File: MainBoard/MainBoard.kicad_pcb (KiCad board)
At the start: 6 copper layers, 45 x 45.6 mm, 56 parts, among them IC1 BQ25171QWDRCRQ1, J1 KH-TYPE-C-16P, U1 STM32L496VGY6PTR, U2 MX25R1635FZUIL0, U3 SI3477DV-T1-GE3, U4 SI3477DV-T1-GE3, U5 TPS63802DLAR, U6 FUSB302BMPX, U7 BNO086, Y1 9HT11-32.768KBZF-T

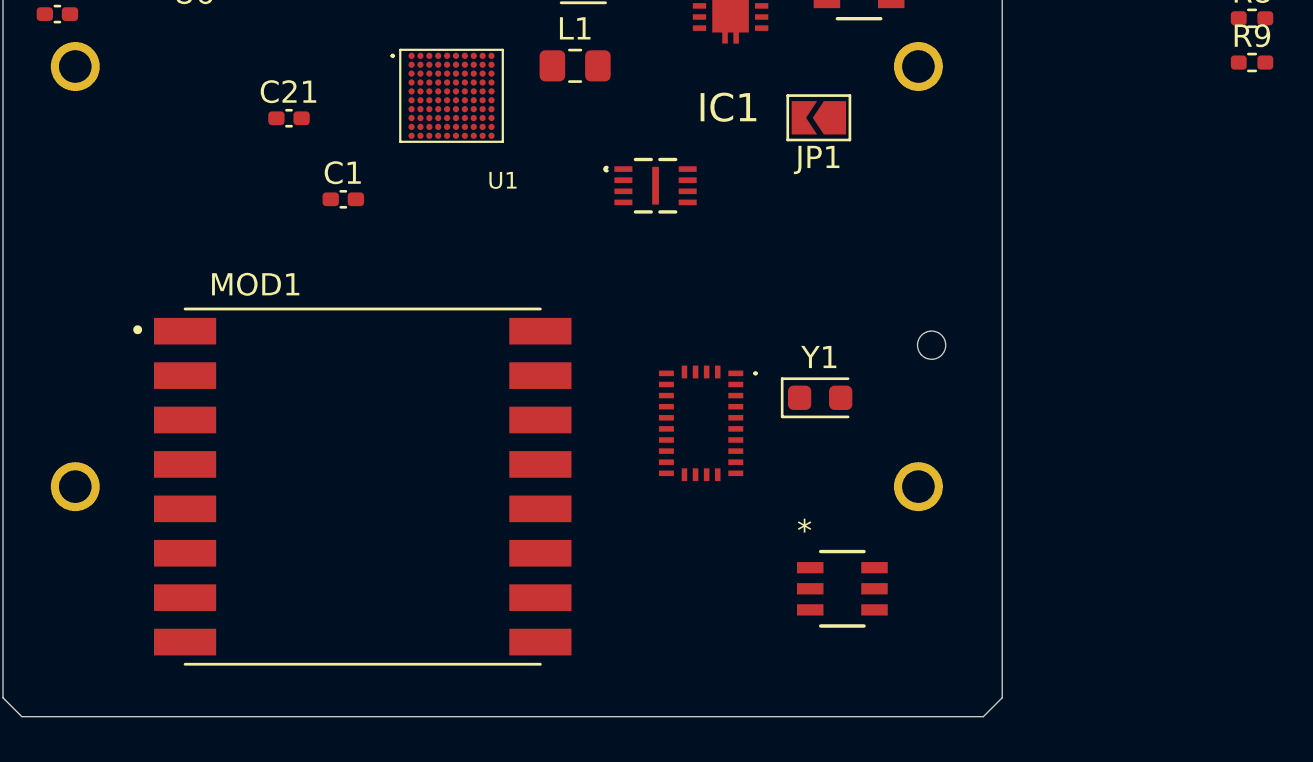
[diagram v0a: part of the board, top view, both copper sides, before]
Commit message: Add CAN transceiver - removed radio module
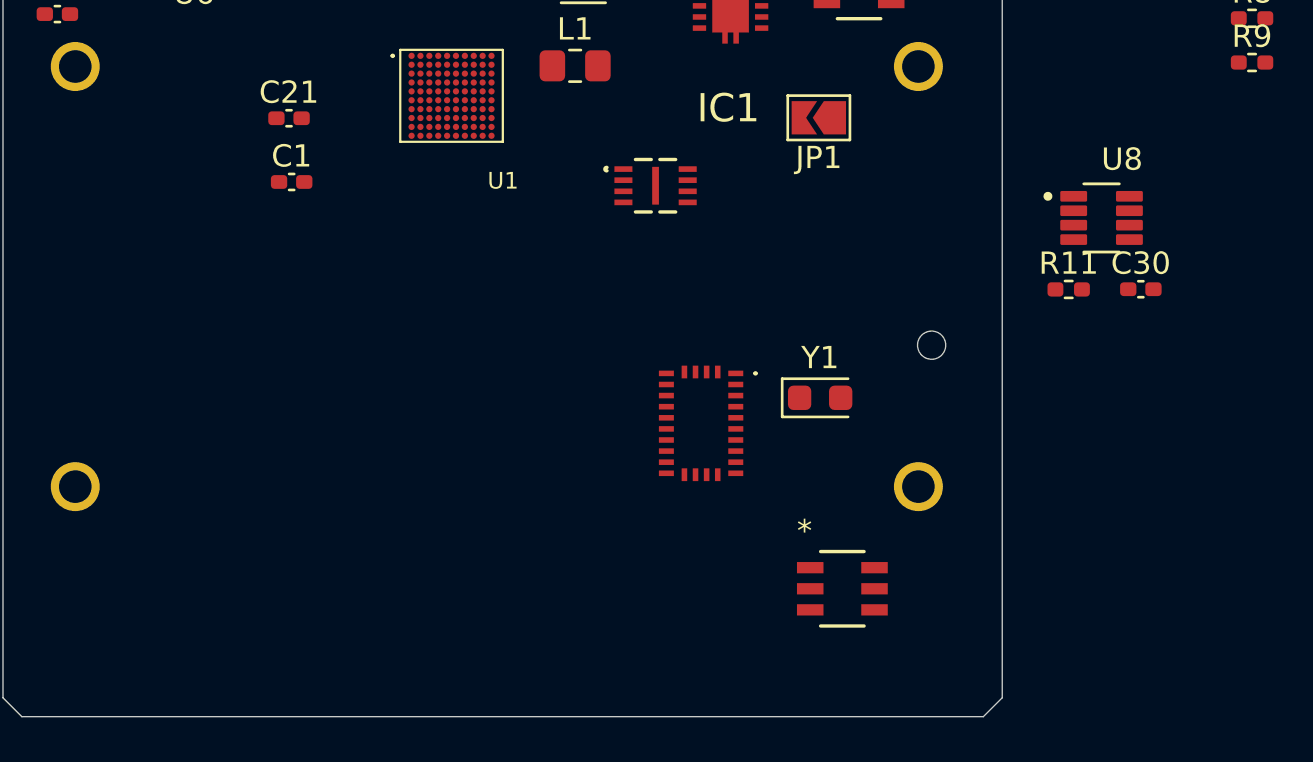
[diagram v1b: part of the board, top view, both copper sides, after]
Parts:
- removed MOD1: RFM98W-433S2, inspirefly:XCVR_RFM98W-433S2
- added C30: 100nF, Capacitor_SMD:C_0402_1005Metric_Pad0.74x0.62mm_HandSolder, F.Cu at (120.6, 67.5)
- added R11: 120, Resistor_SMD:R_0402_1005Metric_Pad0.72x0.64mm_HandSolder, F.Cu at (117.4, 67.5)
- added U8: TCAN332DCNR, inspirefly:SOT65P280X145-8N, F.Cu at (118.9, 64.3)
- moved C1 2.45 mm to (82.4, 62.7)
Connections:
- U1 pad C9: unconnected-(U1A-PC13-PadC9) -> IMU_H_INTN_GPIO
- U1 pad G8: unconnected-(U1A-PA0-PadG8) -> IMU_PS0/WAKE_GPIO
- U7 pad 14: unconnected-(U7-H_INTN-Pad14) -> IMU_H_INTN_GPIO
- U7 pad 6: unconnected-(U7-PS0/WAKE-Pad6) -> IMU_PSO/WAKE_GPIO

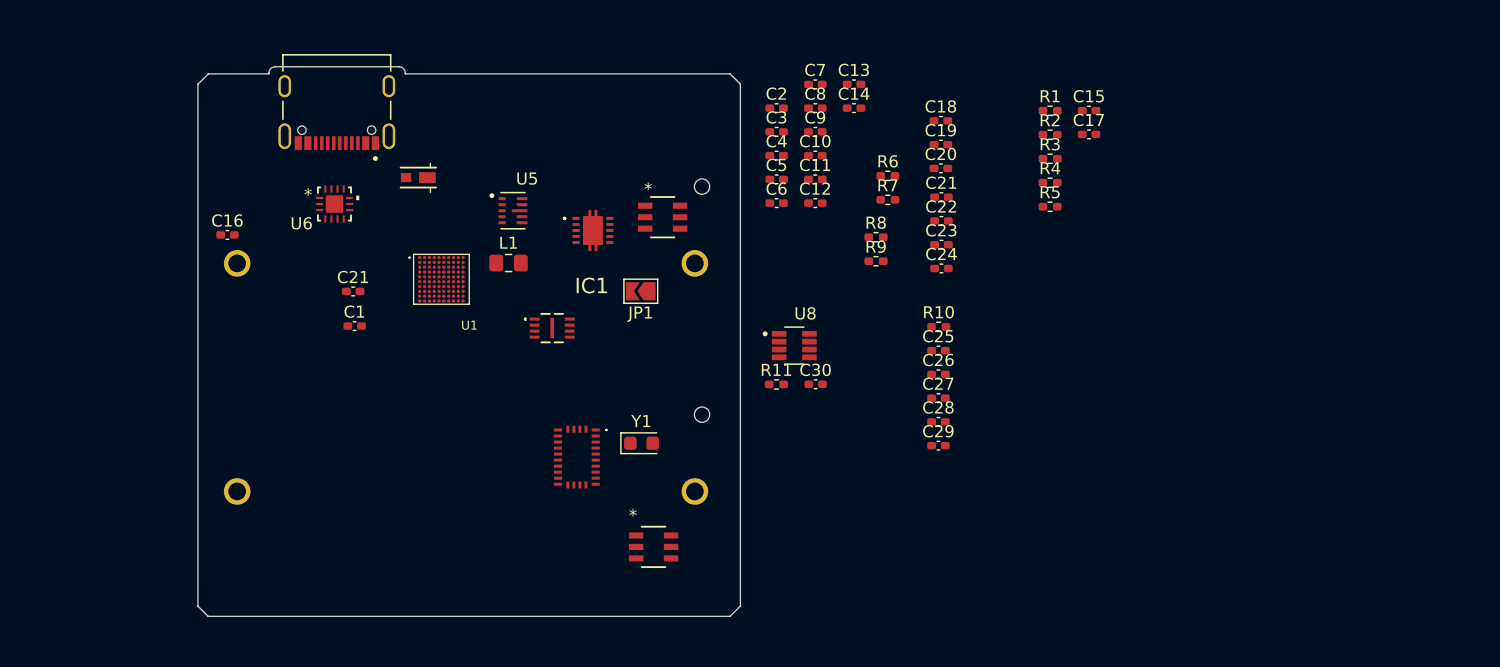
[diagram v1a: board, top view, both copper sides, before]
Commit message: Integrated BQ25756E along with schematic changes
Removed old Battery management, replaced with BQ25756E. Schematic work complete along with external part finding.
Dedicated section to I2C pull ups.
Moved around items in schematics for better look.
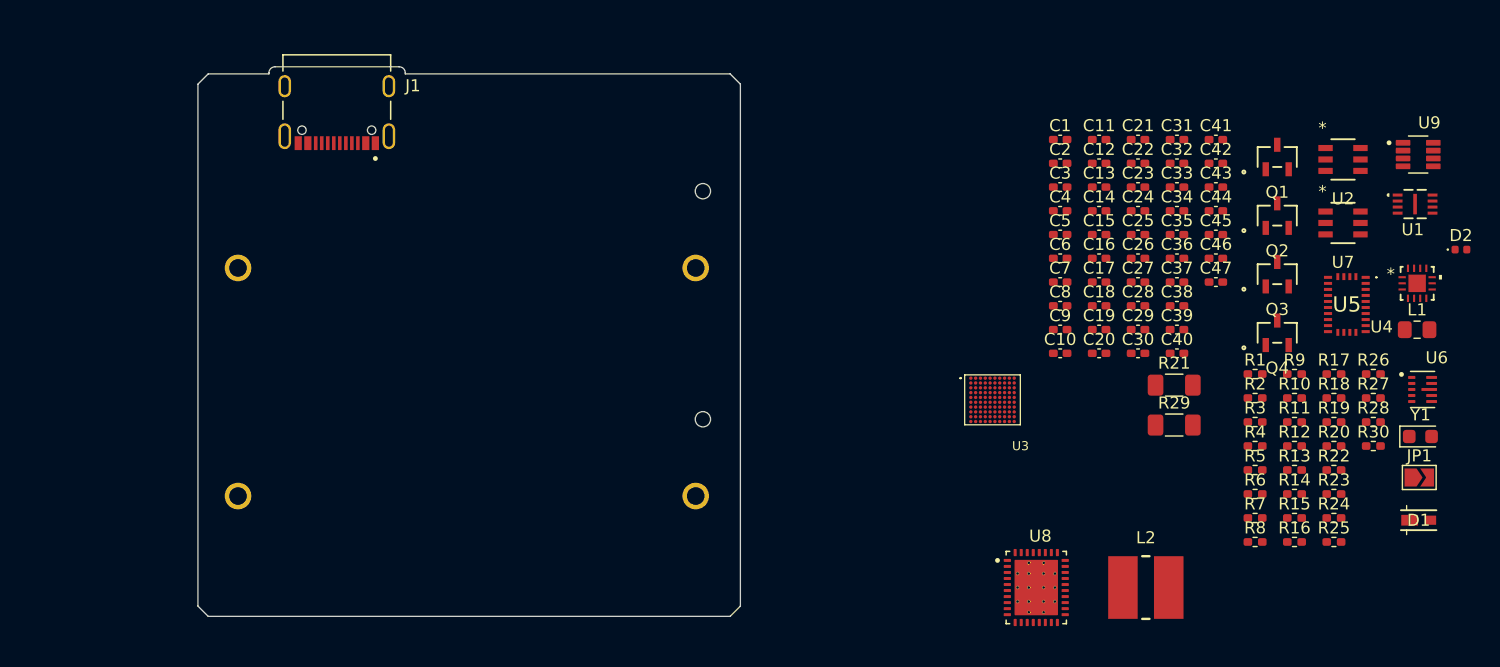
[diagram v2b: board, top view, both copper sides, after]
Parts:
- removed the C21 at (82.3, 59.8)
- removed the C21 at (131.1, 52.0)
- removed IC1: BQ25171QWDRCRQ1, inspirefly:BQ25171QWDRCRQ1
- added C21: 100nF, Capacitor_SMD:C_0402_1005Metric_Pad0.74x0.62mm_HandSolder, F.Cu at (147.4, 47.2)
- added C31: 470nF, Capacitor_SMD:C_0402_1005Metric_Pad0.74x0.62mm_HandSolder, F.Cu at (150.6, 47.2)
- added C32: 100nF, Capacitor_SMD:C_0402_1005Metric_Pad0.74x0.62mm_HandSolder, F.Cu at (150.6, 49.2)
- added C33: 100nF, Capacitor_SMD:C_0402_1005Metric_Pad0.74x0.62mm_HandSolder, F.Cu at (150.6, 51.1)
- added C34: 22uF, Capacitor_SMD:C_0402_1005Metric_Pad0.74x0.62mm_HandSolder, F.Cu at (150.6, 53.1)
- added C35: 22uF, Capacitor_SMD:C_0402_1005Metric_Pad0.74x0.62mm_HandSolder, F.Cu at (150.6, 55.1)
- added C36: 4.7uF, Capacitor_SMD:C_0402_1005Metric_Pad0.74x0.62mm_HandSolder, F.Cu at (150.6, 57.1)
- added C37: 4.7uF, Capacitor_SMD:C_0402_1005Metric_Pad0.74x0.62mm_HandSolder, F.Cu at (150.6, 59.0)
- added C38: 1uF, Capacitor_SMD:C_0402_1005Metric_Pad0.74x0.62mm_HandSolder, F.Cu at (150.6, 61.0)
- added C39: 22uF, Capacitor_SMD:C_0402_1005Metric_Pad0.74x0.62mm_HandSolder, F.Cu at (150.6, 63.0)
- added C40: 22uF, Capacitor_SMD:C_0402_1005Metric_Pad0.74x0.62mm_HandSolder, F.Cu at (150.6, 64.9)
- added C41: 100nF, Capacitor_SMD:C_0402_1005Metric_Pad0.74x0.62mm_HandSolder, F.Cu at (153.8, 47.2)
- added C42: 100nF, Capacitor_SMD:C_0402_1005Metric_Pad0.74x0.62mm_HandSolder, F.Cu at (153.8, 49.2)
- added C43: 100nF, Capacitor_SMD:C_0402_1005Metric_Pad0.74x0.62mm_HandSolder, F.Cu at (153.8, 51.1)
- added C44: 470nF, Capacitor_SMD:C_0402_1005Metric_Pad0.74x0.62mm_HandSolder, F.Cu at (153.8, 53.1)
- added C45: 100nF, Capacitor_SMD:C_0402_1005Metric_Pad0.74x0.62mm_HandSolder, F.Cu at (153.8, 55.1)
- added C46: 22uF, Capacitor_SMD:C_0402_1005Metric_Pad0.74x0.62mm_HandSolder, F.Cu at (153.8, 57.1)
- added C47: 22uF, Capacitor_SMD:C_0402_1005Metric_Pad0.74x0.62mm_HandSolder, F.Cu at (153.8, 59.0)
- added D2: LED, LED_SMD:LED_0402_1005Metric, F.Cu at (174.2, 56.3)
- added L2: 4.7uH, inspirefly:WE-LQSA_5040, F.Cu at (148.0, 84.4)
- added Q1: PMV19XNEAR, inspirefly:TO-236AB_SOT23_NEX, F.Cu at (158.9, 48.7)
- added Q2: PMV19XNEAR, inspirefly:TO-236AB_SOT23_NEX, F.Cu at (158.9, 53.5)
- added Q3: PMV19XNEAR, inspirefly:TO-236AB_SOT23_NEX, F.Cu at (158.9, 58.4)
- added Q4: PMV19XNEAR, inspirefly:TO-236AB_SOT23_NEX, F.Cu at (158.9, 63.2)
- added R12: 50k, Resistor_SMD:R_0402_1005Metric_Pad0.72x0.64mm_HandSolder, F.Cu at (160.4, 72.6)
- added R13: 100K, Resistor_SMD:R_0402_1005Metric_Pad0.72x0.64mm_HandSolder, F.Cu at (160.4, 74.6)
- added R14: 143k, Resistor_SMD:R_0402_1005Metric_Pad0.72x0.64mm_HandSolder, F.Cu at (160.4, 76.6)
- added R15: 250k, Resistor_SMD:R_0402_1005Metric_Pad0.72x0.64mm_HandSolder, F.Cu at (160.4, 78.6)
- added R16: 6.2k, Resistor_SMD:R_0402_1005Metric_Pad0.72x0.64mm_HandSolder, F.Cu at (160.4, 80.6)
- added R17: 36k, Resistor_SMD:R_0402_1005Metric_Pad0.72x0.64mm_HandSolder, F.Cu at (163.6, 66.7)
- added R18: 10, Resistor_SMD:R_0402_1005Metric_Pad0.72x0.64mm_HandSolder, F.Cu at (163.6, 68.7)
- added R19: 25k, Resistor_SMD:R_0402_1005Metric_Pad0.72x0.64mm_HandSolder, F.Cu at (163.6, 70.6)
- added R20: 40k, Resistor_SMD:R_0402_1005Metric_Pad0.72x0.64mm_HandSolder, F.Cu at (163.6, 72.6)
- added R21: 5m, Resistor_SMD:R_1206_3216Metric_Pad1.30x1.75mm_HandSolder, F.Cu at (150.4, 67.6)
- added R22: 250k, Resistor_SMD:R_0402_1005Metric_Pad0.72x0.64mm_HandSolder, F.Cu at (163.6, 74.6)
- added R23: 10, Resistor_SMD:R_0402_1005Metric_Pad0.72x0.64mm_HandSolder, F.Cu at (163.6, 76.6)
- added R24: 10k, Resistor_SMD:R_0402_1005Metric_Pad0.72x0.64mm_HandSolder, F.Cu at (163.6, 78.6)
- added R25: 120, Resistor_SMD:R_0402_1005Metric_Pad0.72x0.64mm_HandSolder, F.Cu at (163.6, 80.6)
- added R26: 10k, Resistor_SMD:R_0402_1005Metric_Pad0.72x0.64mm_HandSolder, F.Cu at (166.9, 66.7)
- added R27: 10, Resistor_SMD:R_0402_1005Metric_Pad0.72x0.64mm_HandSolder, F.Cu at (166.9, 68.7)
- added R28: 10, Resistor_SMD:R_0402_1005Metric_Pad0.72x0.64mm_HandSolder, F.Cu at (166.9, 70.6)
- added R29: 5m, Resistor_SMD:R_1206_3216Metric_Pad1.30x1.75mm_HandSolder, F.Cu at (150.4, 70.9)
- added R30: 10, Resistor_SMD:R_0402_1005Metric_Pad0.72x0.64mm_HandSolder, F.Cu at (166.9, 72.6)
- added U9: TCAN332DCNR, inspirefly:SOT65P280X145-8N, F.Cu at (170.6, 48.5)
- C1, C16: value 100nF -> 1uF
- C11: value 100nF -> 4.7uF
- C12, C13, C15, C17: value 1uF -> 100nF
- C19: value 10uF -> 1uF
- C20: value 10uF -> 100nF
- C23: value 470pF -> 100nF
- C24: value 470pF -> 22pF
- C25: value 100nF -> 22pF
- C26, C27: value 100nF -> 10uF
- C28, C29: value 22pF -> 22uF
- C6: value 100nF -> 470pF
- C7: value 4.7uF -> 470pF
- R1: value 10k -> 2.2k
- R11: value 120 -> 280k
- R2: value 375 -> 2.2k
- R3: value 18k -> 2.2k
- R4: value 62k -> 2.2k
- R5: value 100K -> 2.2k
- R6: value 280k -> 2.2k
- R7: value 50k -> 2.2k
- R8, R9: value 4.7k -> 2.2k
- U1: value STM32L496VGY6PTR -> MX25R1635FZUIL0; footprint inspirefly:STM32L496VGY6TR -> inspirefly:USON-8L-2X3X0P6_MAC
- U2: value MX25R1635FZUIL0 -> SI3477DV-T1-GE3; footprint inspirefly:USON-8L-2X3X0P6_MAC -> inspirefly:SOT_V-T1-GE3_VIS-M
- U3: value SI3477DV-T1-GE3 -> STM32L496VGY6PTR; footprint inspirefly:SOT_V-T1-GE3_VIS-M -> inspirefly:STM32L496VGY6TR
- U4: value SI3477DV-T1-GE3 -> FUSB302BMPX; footprint inspirefly:SOT_V-T1-GE3_VIS-M -> inspirefly:MLP14_2P5X2P5_ONS
- U5: value TPS63802DLAR -> BNO086; footprint inspirefly:VREG_TPS63802DLAR -> inspirefly:BNO086
- U6: value FUSB302BMPX -> TPS63802DLAR; footprint inspirefly:MLP14_2P5X2P5_ONS -> inspirefly:VREG_TPS63802DLAR
- U7: value BNO086 -> SI3477DV-T1-GE3; footprint inspirefly:BNO086 -> inspirefly:SOT_V-T1-GE3_VIS-M
- U8: value TCAN332DCNR -> BQ25756ERRVR; footprint inspirefly:SOT65P280X145-8N -> inspirefly:IC_BQ25756ERRVR
- moved U6 91.6 mm to (171.0, 67.9)
- moved D1 87.7 mm to (170.7, 78.8), turned to 0 degrees
- moved U1 81.0 mm to (170.4, 52.6)
- moved L1 75.6 mm to (170.5, 63.0)
- moved C16 72.3 mm to (144.2, 57.1)
- moved U5 69.6 mm to (164.7, 60.9)
- moved U2 67.1 mm to (164.4, 48.9)
- moved U4 67.0 mm to (170.5, 59.1)
- moved U7 66.5 mm to (164.4, 54.1)
- moved JP1 66.4 mm to (170.7, 75.2), turned to 0 degrees
- moved Y1 64.6 mm to (170.8, 71.8)
- moved C1 60.5 mm to (140.9, 47.2)
- moved R11 43.1 mm to (160.4, 70.6)
- moved R8 40.3 mm to (157.1, 80.6)
- moved R6 40.3 mm to (157.1, 76.6)
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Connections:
- BT1 pad P: Net-(U3-S) -> Net-(U7-S)
- BT2 pad P: Net-(U3-S) -> Net-(U7-S)
- C15 pad 1: EXTERNAL_VOLTAGE -> +3.3V
- C16 pad 1: GND -> +3.3V
- C16 pad 2: +3.3V -> GND
- C17 pad 1: BAT+ -> +3.3V
- C23 pad 1: Net-(J1-CC2) -> +3.3V
- C24 pad 1: Net-(J1-CC1) -> Net-(U5-XOUT32/CLKSEL1)
- C25 pad 2: +3.3V -> Net-(U5-XIN32)
- C27 pad 1: Net-(U7-CAP) -> +3.3V
- C28 pad 1: Net-(U7-XOUT32/CLKSEL1) -> EXTERNAL_VOLTAGE
- C29 pad 1: GND -> EXTERNAL_VOLTAGE
- C29 pad 2: Net-(U7-XIN32) -> GND
- C3 pad 1: +3.3V -> GND
- C3 pad 2: GND -> +3.3V
- C30 pad 1: +3.3V -> ACP
- C4 pad 1: +3.3V -> Net-(U5-CAP)
- C5 pad 1: +3.3V -> GND
- C5 pad 2: GND -> +3.3V
- C6 pad 1: +3.3V -> Net-(J1-CC2)
- C7 pad 1: +3.3V -> Net-(J1-CC1)
- L1 pad 1: Net-(U5-L1) -> Net-(U6-L1)
- L1 pad 2: Net-(U5-L2) -> Net-(U6-L2)
- R1 pad 1: GND -> +3.3V
- R1 pad 2: Net-(IC1-TS) -> I2C1_SDA
- R11 pad 1: CAN_L -> +3.3V
- R11 pad 2: CAN_H -> Net-(U6-FB)
- R2 pad 1: GND -> I2C1_SCL
- R2 pad 2: Net-(IC1-ISET) -> +3.3V
- R3 pad 1: Net-(IC1-VSET) -> +3.3V
- R3 pad 2: GND -> I2C2_SDA
- R4 pad 1: Net-(IC1-CHM_TMR) -> I2C2_SCL
- R4 pad 2: GND -> +3.3V
- R5 pad 1: BAT_PULLDOWN -> +3.3V
- R5 pad 2: Net-(U3-S) -> I2C3_SDA
- R6 pad 1: +3.3V -> I2C3_SCL
- R6 pad 2: Net-(U5-FB) -> +3.3V
- R7 pad 1: Net-(U5-FB) -> +3.3V
- R7 pad 2: GND -> I2C3_SDA
- R8 pad 1: I2C1_SCL -> INT_N
- R8 pad 2: GND -> +3.3V
- R9 pad 1: GND -> I2C3_SCL
- R9 pad 2: I2C1_SDA -> +3.3V
- U2 pad 1: QUADSPI_BK2_NCS -> unconnected-(U2-D-Pad1)
- U2 pad 2: QUADSPI_BK2_IO1 -> unconnected-(U2-D-Pad2)
- U2 pad 3: QUADSPI_BK2_IO2 -> unconnected-(U2-G-Pad3)
- U2 pad 4: GND -> unconnected-(U2-S-Pad4)
- U2 pad 5: QUADSPI_BK2_IO0 -> unconnected-(U2-D-Pad5)
- U2 pad 6: QUADSPI_CLK -> unconnected-(U2-D-Pad6)
- U4 pad 2: unconnected-(U4-D-Pad2) -> Net-(D1-A)
- U4 pad 3: unconnected-(U4-G-Pad3) -> +3.3V
- U4 pad 4: unconnected-(U4-S-Pad4) -> +3.3V
- U4 pad 5: unconnected-(U4-D-Pad5) -> INT_N
- U4 pad 6: unconnected-(U4-D-Pad6) -> I2C1_SCL
- U5 pad 1: BAT+ -> unconnected-(U5-RESV_NC_1-Pad1)
- U5 pad 10: BAT+ -> unconnected-(U5-CLKSEL0-Pad10)
- U5 pad 3: GND -> +3.3V
- U5 pad 4: Net-(U5-FB) -> IMU_BOOTN
- U5 pad 5: unconnected-(U5-PG-Pad5) -> +3.3V
- U5 pad 6: +3.3V -> IMU_PSO/WAKE_GPIO
- U5 pad 7: Net-(U5-L2) -> unconnected-(U5-RESV_NC_2-Pad7)
- U5 pad 8: GND -> unconnected-(U5-RESV_NC_3-Pad8)
- U5 pad 9: Net-(U5-L1) -> Net-(U5-CAP)
- U6 pad 1: unconnected-(U6-CC2-Pad1) -> BAT+
- U6 pad 10: unconnected-(U6-CC1-Pad10) -> BAT+
- U6 pad 2: Net-(D1-A) -> GND
- U6 pad 3: +3.3V -> GND
- U6 pad 4: +3.3V -> Net-(U6-FB)
- U6 pad 6: I2C1_SCL -> +3.3V
- U6 pad 7: I2C1_SDA -> Net-(U6-L2)
- U6 pad 9: GND -> Net-(U6-L1)
- U7 pad 1: unconnected-(U7-RESV_NC_1-Pad1) -> BAT+
- U7 pad 2: GND -> BAT+
- U7 pad 3: +3.3V -> BAT_PULLDOWN
- U7 pad 4: IMU_BOOTN -> Net-(U7-S)
- U7 pad 5: +3.3V -> BAT+
- U7 pad 6: IMU_PSO/WAKE_GPIO -> BAT+
- U8 pad 1: CAN_TXD -> I2C2_SCL
- U8 pad 2: GND -> I2C2_SDA
- U8 pad 3: +3.3V -> BQ_INT_DIN
- U8 pad 4: CAN_RXD -> unconnected-(U8-STAT1-Pad4)
- U8 pad 6: CAN_L -> Net-(U8-~{PG})
- U8 pad 7: CAN_H -> GND
- U8 pad 8: unconnected-(U8-NC_8-Pad8) -> THERMISTOR_FEEDBACK
- Y1 pad 1: Net-(U7-XIN32) -> Net-(U5-XIN32)
- Y1 pad 2: Net-(U7-XOUT32/CLKSEL1) -> Net-(U5-XOUT32/CLKSEL1)

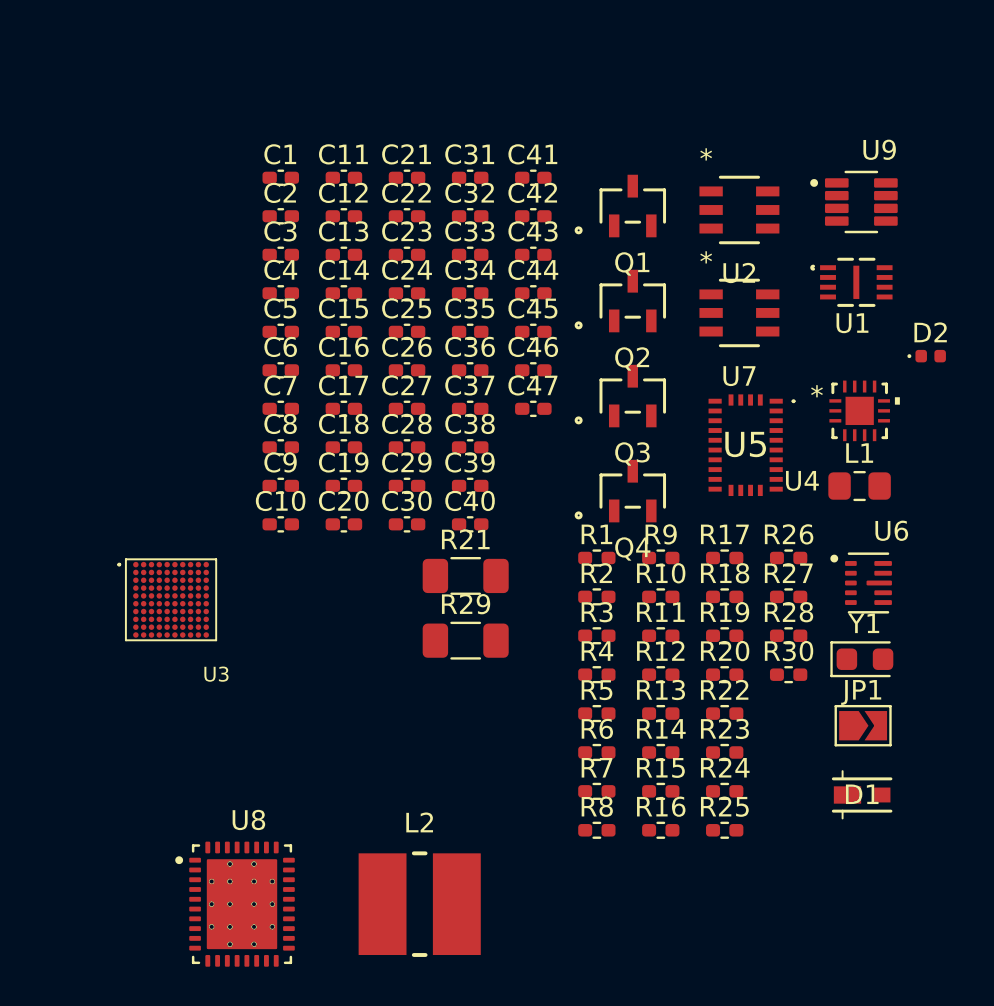
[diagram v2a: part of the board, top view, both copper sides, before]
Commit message: Changed bulk cap values
Removed parallel 22uF 0402 for bulks on battery management. Replaced with 47uF 1206 due to over voltage issues.
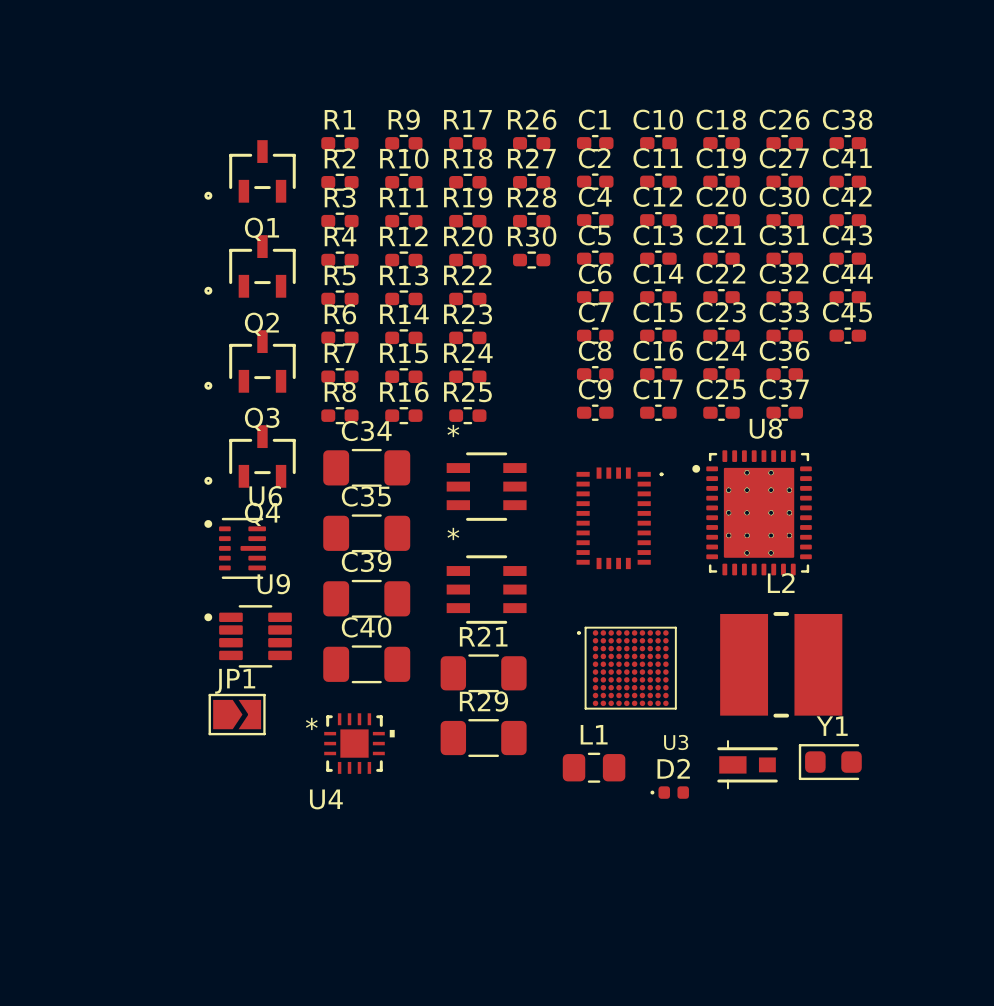
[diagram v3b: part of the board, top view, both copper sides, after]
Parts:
- removed C28, C29, C46, C47: 22uF, Capacitor_SMD:C_0402_1005Metric_Pad0.74x0.62mm_HandSolder
- removed C3: 100nF, Capacitor_SMD:C_0402_1005Metric_Pad0.74x0.62mm_HandSolder
- removed U1: MX25R1635FZUIL0, inspirefly:USON-8L-2X3X0P6_MAC
- C34, C35, C39, C40: value 22uF -> 47uF; footprint Capacitor_SMD:C_0402_1005Metric_Pad0.74x0.62mm_HandSolder -> Capacitor_SMD:C_1206_3216Metric_Pad1.33x1.80mm_HandSolder
- moved U9 38.1 mm to (139.6, 70.7)
- moved U8 33.2 mm to (165.4, 64.3)
- moved U6 32.1 mm to (139.0, 66.2)
- moved JP1 32.0 mm to (138.7, 74.7)
- moved U4 30.9 mm to (144.7, 76.2)
- moved C10 27.4 mm to (160.2, 45.4)
- moved D2 25.9 mm to (161.0, 78.7)
- moved R10 25.0 mm to (147.2, 47.4)
- moved R13 25.0 mm to (147.2, 53.4)
- moved R27 25.0 mm to (153.8, 47.4)
- moved R11 25.0 mm to (147.2, 49.4)
- moved R14 25.0 mm to (147.2, 55.4)
- moved R16 25.0 mm to (147.2, 59.4)
- moved R28 25.0 mm to (153.8, 49.4)
- moved R12 25.0 mm to (147.2, 51.4)
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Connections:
- C34 pad 1: Net-(Q1-D) -> Net-(Q3-D)
- C39 pad 1: Net-(Q3-D) -> BAT+
- C40 pad 1: Net-(Q3-D) -> EXTERNAL_VOLTAGE
- U3 pad D4: QUADSPI_BK2_NCS -> unconnected-(U3A-PC11-PadD4)
- U3 pad F6: QUADSPI_BK2_IO2 -> unconnected-(U3A-PC3-PadF6)
- U3 pad F7: QUADSPI_BK2_IO0 -> unconnected-(U3A-PC1-PadF7)
- U3 pad G9: QUADSPI_BK2_IO1 -> unconnected-(U3A-PC2-PadG9)
- U3 pad J9: QUADSPI_CLK -> unconnected-(U3A-PA3-PadJ9)
- U3 pad K8: QUADSPI_BK2_IO3 -> unconnected-(U3A-PC4-PadK8)
